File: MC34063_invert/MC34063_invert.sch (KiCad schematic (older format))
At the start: 23 parts, among them J1 INPUT, J2 OUTPUT, Q1 BC557, U1 MC34063AP

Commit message: Gerbers
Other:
- moved on the sheet: D1
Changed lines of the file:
@@
 	4400 3000 4700 3000
-Wire Wire Line
-	4400 3100 5000 3100
 Wire Wire Line
 	3350 3300 3600 3300
@@
 F 3 "~" H 3350 3450 50  0001 C CNN
 	1    3350 3450
-	1    0    0    -1
-$EndComp
-$Comp
-L Device:D D1
-U 1 1 639830CC
-P 5450 3150
-F 0 "D1" H 5450 2933 50  0000 C CNN
-F 1 "1N5817" H 5450 3024 50  0000 C CNN
-F 2 "Diode_THT:D_A-405_P7.62mm_Horizontal" H 5450 3150 50  0001 C CNN
-F 3 "~" H 5450 3150 50  0001 C CNN
-	1    5450 3150
 	1    0    0    -1
 $EndComp
@@
 Wire Wire Line
 	5500 3550 5500 3400
-Wire Wire Line
-	5500 3400 5650 3400
 NoConn ~ 5450 3400
 $Comp
@@
 $EndComp
 Wire Wire Line
-	5650 3150 5650 3400
-Wire Wire Line
-	5600 3150 5650 3150
-Wire Wire Line
 	4400 3150 4400 3300
-Wire Wire Line
-	4400 3150 5300 3150
 Connection ~ 4400 3300
 Wire Wire Line
@@
 	0    -1   -1   0
 $EndComp
+Wire Wire Line
+	5500 3400 5650 3400
+Wire Wire Line
+	4400 3100 5000 3100
+$Comp
+L Device:D D1
+U 1 1 639830CC
+P 5400 2900
+F 0 "D1" H 5400 2683 50  0000 C CNN
+F 1 "1N5817" H 5400 2774 50  0000 C CNN
+F 2 "Diode_THT:D_A-405_P7.62mm_Horizontal" H 5400 2900 50  0001 C CNN
+F 3 "~" H 5400 2900 50  0001 C CNN
+	1    5400 2900
+	1    0    0    1
+$EndComp
+Wire Wire Line
+	5550 2900 5650 2900
+Wire Wire Line
+	5650 2900 5650 3400
+Wire Wire Line
+	5250 2900 5150 2900
+Wire Wire Line
+	5150 2900 5150 3150
+Wire Wire Line
+	5150 3150 4400 3150
 $EndSCHEMATC

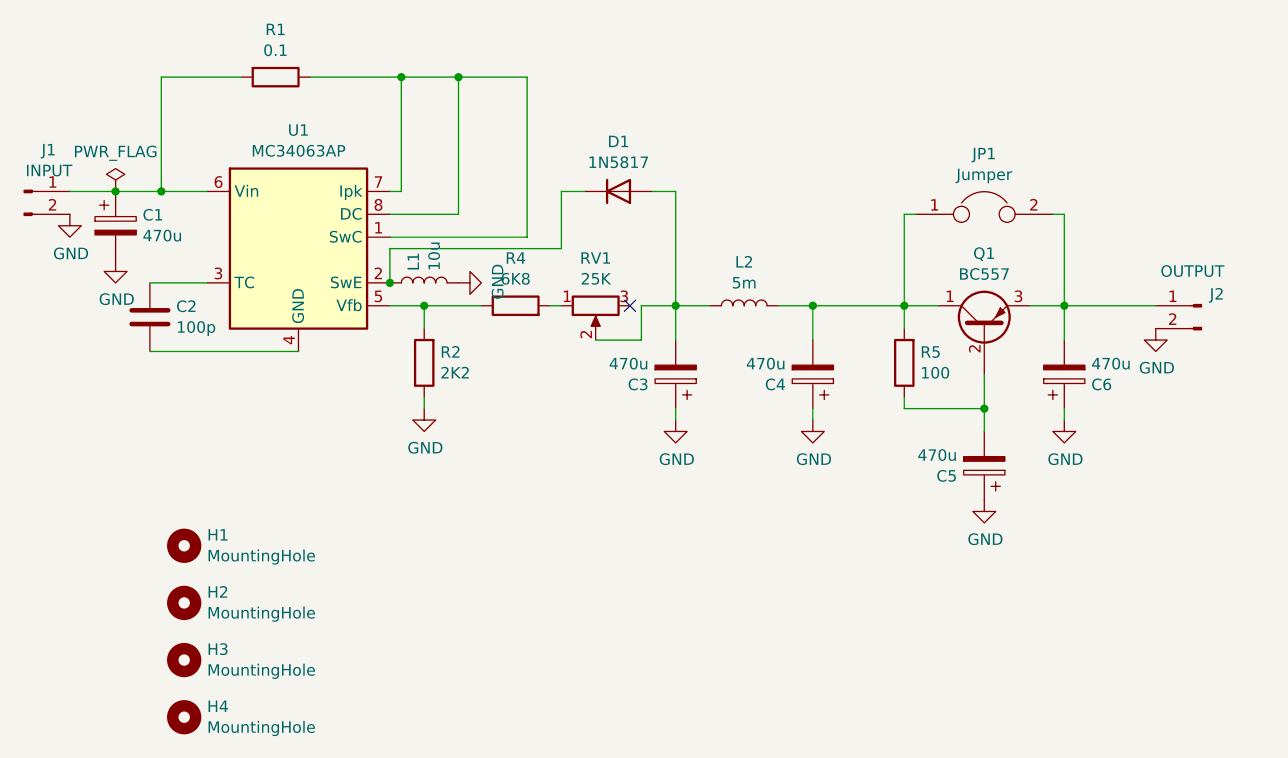
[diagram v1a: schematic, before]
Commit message: Fixed error in feedback loop
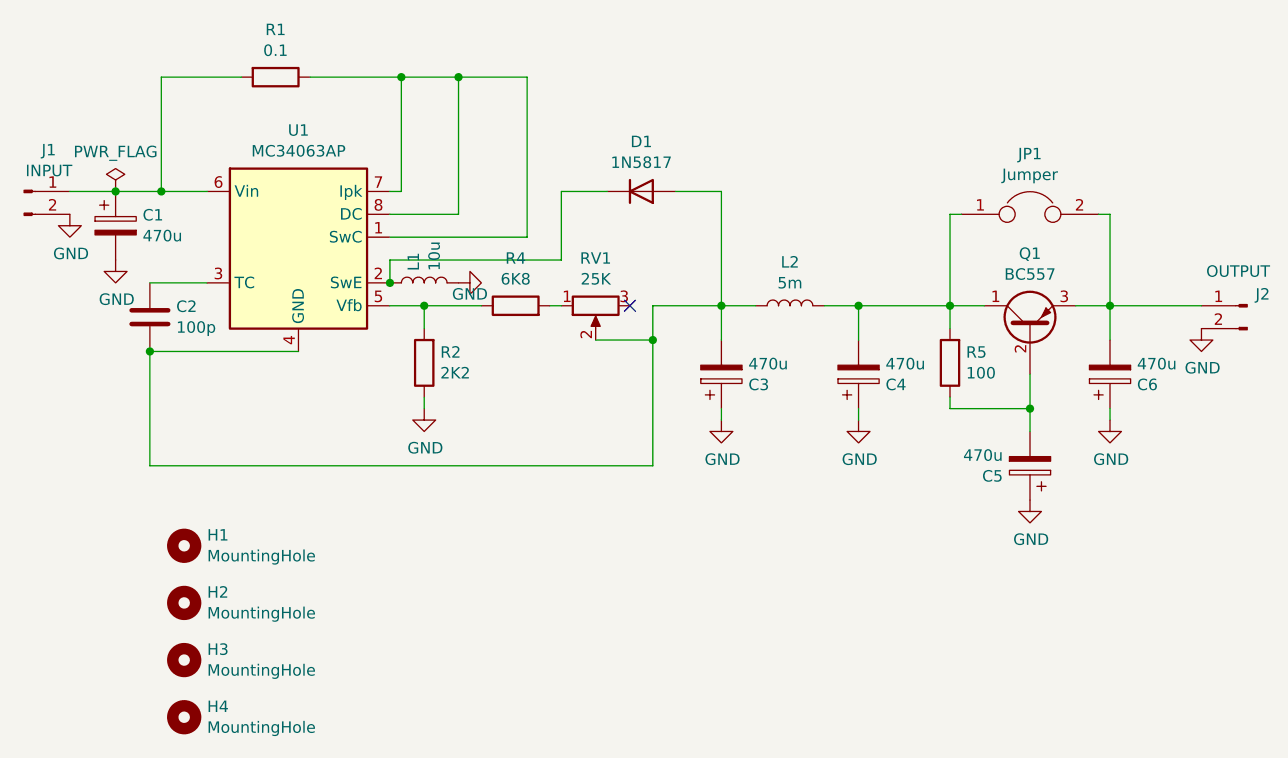
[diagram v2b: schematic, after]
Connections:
- net at C2.2, U1.4 (GND): now also C3.2, D1.2 (A), L2.1, RV1.2
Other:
- moved on the sheet: C3, C4, C5, C6, D1, J2, JP1, L2, Q1, R5

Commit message: Made buck & inverter PCB's smaller for panelization
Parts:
- Q1: value BC557 -> 2N2907; symbol Transistor_BJT:BC557 -> Transistor_BJT:2N3905
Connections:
- net at C6.2, J2.1 (Pin_1), JP1.2: now also Q1.1 (E); no longer Q1.3 (E)
- net at C4.2, JP1.1, L2.2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: now also Q1.3 (C); no longer Q1.1 (C)
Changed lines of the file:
@@
 	5850 2900 5850 3400
 $Comp
-L Transistor_BJT:BC557 Q1
+L Transistor_BJT:2N3905 Q1
 U 1 1 63970457
 P 7200 3500
 F 0 "Q1" V 7528 3500 50  0000 C CNN
-F 1 "BC557" V 7437 3500 50  0000 C CNN
+F 1 "2N2907" V 7437 3500 50  0000 C CNN
 F 2 "Package_TO_SOT_THT:TO-92_Inline" H 7400 3425 50  0001 L CIN
 F 3 "https://www.onsemi.com/pub/Collateral/BC556BTA-D.pdf" H 7200 3500 50  0001 L CNN
